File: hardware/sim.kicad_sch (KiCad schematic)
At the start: 11 parts, among them J14 PRPC006SAAN-RC, J15 G85D1160022HHR

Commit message: HW: Layout SIM section
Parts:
- removed J15: G85D1160022HHR, G85D1160022HHR:AMPHENOL_G85D1160022HHR, symbol Connector:SIM_Card
- added J15: G85D1160022HHR, G85D1160022HHR:AMPHENOL_G85D1160022HHR, symbol G85D1160022HHR:G85D1160022HHR
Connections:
- net GND: now also J15.C5 (GND), J15.S1 (SH), J15.S2 (SH), J15.S3 (SH)
- net SIM_CLK: now also J15.C3 (CLK)
- net SIM_IO: now also J15.C7 (I/O)
- net SIM_RST: now also J15.C2 (RST)
- net VSIM: now also J15.C1 (VCC)
- no-connect marks 1 -> 2
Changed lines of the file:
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@@
 	)
 	(junction
+		(at 187.96 134.62)
+		(diameter 0)
+		(color 0 0 0 0)
+	)
+	(junction
 		(at 182.88 119.38)
 		(diameter 0)
@@
 		(at 189.23 129.54)
 	)
+	(no_connect
+		(at 189.23 137.16)
+	)
 	(wire
 		(pts
@@
 	(wire
 		(pts
-			(xy 187.96 127) (xy 187.96 144.78)
+			(xy 187.96 127) (xy 187.96 134.62)
 		)
 		(stroke
@@
 	(wire
 		(pts
+			(xy 187.96 134.62) (xy 189.23 134.62)
+		)
+		(stroke
+			(width 0)
+			(type default)
+		)
+	)
+	(wire
+		(pts
 			(xy 189.23 127) (xy 187.96 127)
 		)
@@
 	(wire
 		(pts
+			(xy 187.96 134.62) (xy 187.96 144.78)
+		)
+		(stroke
+			(width 0)
+			(type default)
+		)
+	)
+	(wire
+		(pts
 			(xy 156.21 144.78) (xy 165.1 144.78)
 		)
@@
 	)
 	(symbol
-		(lib_id "Device:D_Zener")
-		(at 182.88 137.16 90)
-		(mirror x)
+		(lib_id "G85D1160022HHR:G85D1160022HHR")
+		(at 204.47 116.84 0)
 		(unit 1)
 		(exclude_from_sim no)
@@
 		(on_board yes)
 		(dnp no)
-		(property "Reference" "TVS15"
-			(at 178.435 137.16 90)
+		(property "Reference" "J15"
+			(at 202.692 116.84 0)
 			(effects
 				(font
 					(size 1.27 1.27)
 				)
+				(justify left)
 			)
 		)
-		(property "Value" "CPDUC5V0USP-HF"
-			(at 172.72 138.43 90)
+		(property "Value" "G85D1160022HHR"
+			(at 195.834 139.7 0)
 			(effects
 				(font
 					(size 1.27 1.27)
 				)
-				(hide yes)
+				(justify left)
 			)
 		)
-		(property "Footprint" "Diode_SMD:D_0603_1608Metric_Pad1.05x0.95mm_HandSolder"
-			(at 182.88 137.16 0)
+		(property "Footprint" "G85D1160022HHR:AMPHENOL_G85D1160022HHR"
+			(at 204.47 116.84 0)
 			(effects
 				(font
@@
 			)
 		)
-		(property "Datasheet" "~"
-			(at 182.88 137.16 0)
+		(property "Datasheet" "https://cdn.amphenol-cs.com/media/wysiwyg/files/drawing/g85d1160x22hhr.pdf"
+			(at 204.47 116.84 0)
 			(effects
 				(font
@@
 			)
 		)
-		(property "Description" ""
-			(at 182.88 137.16 0)
+		(property "Description" "NANO SIM HING GF"
+			(at 204.47 116.84 0)
 			(effects
 				(font
@@
 			)
 		)
-		(property "Digi-Key Part Number" "641-1765-1-ND"
-			(at 182.88 137.16 0)
+		(property "Digi-Key Part Number" "664-G85D1160022HHRCT-ND"
+			(at 204.47 116.84 0)
 			(effects
 				(font
@@
 			)
 		)
-		(property "Manufacturer" "Comchip Technology"
-			(at 182.88 137.16 0)
+		(property "Manufacturer" "Amphenol ICC (Commercial Products)"
+			(at 204.47 116.84 0)
 			(effects
 				(font
@@
 			)
 		)
-		(property "Manufacturer Part Number" "CPDUC5V0USP-HF"
-			(at 182.88 137.16 0)
+		(property "Manufacturer Part Number" "G85D1160022HHR"
+			(at 204.47 116.84 0)
 			(effects
 				(font
@@
 			)
 		)
-		(pin "2"
+		(pin "S2"
 		)
-		(pin "1"
+		(pin "C1"
+		)
+		(pin "C3"
+		)
+		(pin "C6"
+		)
+		(pin "C7"
+		)
+		(pin "SW"
+		)
+		(pin "C5"
+		)
+		(pin "S1"
+		)
+		(pin "S3"
+		)
+		(pin "C2"
 		)
 		(instances
-			(project "iida_devkit"
+			(project ""
 				(path "/b12a6e25-97fb-4aba-bc96-af8db389bb9a/33580d9f-a609-4568-baaf-9a29cf2dabcd"
-					(reference "TVS15")
+					(reference "J15")
 					(unit 1)
 				)
@@
 	(symbol
 		(lib_id "Device:D_Zener")
-		(at 156.21 137.16 90)
+		(at 182.88 137.16 90)
 		(mirror x)
 		(unit 1)
@@
 		(on_board yes)
 		(dnp no)
-		(property "Reference" "TVS12"
-			(at 151.765 137.16 90)
+		(property "Reference" "TVS15"
+			(at 178.435 137.16 90)
 			(effects
 				(font
@@
 		)
 		(property "Value" "CPDUC5V0USP-HF"
-			(at 146.05 138.43 90)
+			(at 172.72 138.43 90)
 			(effects
 				(font
@@
 		)
 		(property "Footprint" "Diode_SMD:D_0603_1608Metric_Pad1.05x0.95mm_HandSolder"
-			(at 156.21 137.16 0)
+			(at 182.88 137.16 0)
 			(effects
 				(font
@@
 		)
 		(property "Datasheet" "~"
-			(at 156.21 137.16 0)
+			(at 182.88 137.16 0)
 			(effects
 				(font
@@
 		)
 		(property "Description" ""
-			(at 156.21 137.16 0)
+			(at 182.88 137.16 0)
 			(effects
 				(font
@@
 		)
 		(property "Digi-Key Part Number" "641-1765-1-ND"
-			(at 156.21 137.16 0)
+			(at 182.88 137.16 0)
 			(effects
 				(font
@@
 		)
 		(property "Manufacturer" "Comchip Technology"
-			(at 156.21 137.16 0)
+			(at 182.88 137.16 0)
 			(effects
 				(font
@@
 		)
 		(property "Manufacturer Part Number" "CPDUC5V0USP-HF"
-			(at 156.21 137.16 0)
+			(at 182.88 137.16 0)
 			(effects
 				(font
@@
 			(project "iida_devkit"
 				(path "/b12a6e25-97fb-4aba-bc96-af8db389bb9a/33580d9f-a609-4568-baaf-9a29cf2dabcd"
-					(reference "TVS12")
+					(reference "TVS15")
 					(unit 1)
 				)
@@
 	)
 	(symbol
-		(lib_id "Device:C")
-		(at 121.92 137.16 0)
+		(lib_id "Device:D_Zener")
+		(at 156.21 137.16 90)
+		(mirror x)
 		(unit 1)
 		(exclude_from_sim no)
@@
 		(on_board yes)
 		(dnp no)
-		(property "Reference" "C35"
-			(at 119.38 135.89 0)
+		(property "Reference" "TVS12"
+			(at 151.765 137.16 90)
 			(effects
 				(font
 					(size 1.27 1.27)
 				)
-				(justify right)
 			)
 		)
-		(property "Value" "33 pF"
-			(at 119.38 138.43 0)
+		(property "Value" "CPDUC5V0USP-HF"
+			(at 146.05 138.43 90)
 			(effects
 				(font
 					(size 1.27 1.27)
 				)
-				(justify right)
+				(hide yes)
 			)
 		)
-		(property "Footprint" "Capacitor_SMD:C_0603_1608Metric_Pad1.08x0.95mm_HandSolder"
-			(at 122.8852 140.97 0)
+		(property "Footprint" "Diode_SMD:D_0603_1608Metric_Pad1.05x0.95mm_HandSolder"
+			(at 156.21 137.16 0)
 			(effects
 				(font
@@
 		)
 		(property "Datasheet" "~"
-			(at 121.92 137.16 0)
+			(at 156.21 137.16 0)
 			(effects
 				(font
@@
 		)
 		(property "Description" ""
-			(at 121.92 137.16 0)
+			(at 156.21 137.16 0)
 			(effects
 				(font
@@
 			)
 		)
-		(property "Digi-Key Part Number" "732-7749-1-ND"
-			(at 121.92 137.16 0)
+		(property "Digi-Key Part Number" "641-1765-1-ND"
+			(at 156.21 137.16 0)
 			(effects
 				(font
@@
 			)
 		)
-		(property "Manufacturer" "Würth Elektronik"
-			(at 121.92 137.16 0)
+		(property "Manufacturer" "Comchip Technology"
+			(at 156.21 137.16 0)
 			(effects
 				(font
@@
 			)
 		)
-		(property "Manufacturer Part Number" "885012006005"
-			(at 121.92 137.16 0)
+		(property "Manufacturer Part Number" "CPDUC5V0USP-HF"
+			(at 156.21 137.16 0)
 			(effects
 				(font
@@
 			(project "iida_devkit"
 				(path "/b12a6e25-97fb-4aba-bc96-af8db389bb9a/33580d9f-a609-4568-baaf-9a29cf2dabcd"
-					(reference "C35")
+					(reference "TVS12")
 					(unit 1)
 				)
@@
 	)
 	(symbol
-		(lib_id "Connector:SIM_Card")
-		(at 201.93 127 0)
+		(lib_id "Device:C")
+		(at 121.92 137.16 0)
 		(unit 1)
 		(exclude_from_sim no)
@@
 		(on_board yes)
 		(dnp no)
-		(property "Reference" "J15"
-			(at 204.47 114.808 0)
+		(property "Reference" "C35"
+			(at 119.38 135.89 0)
 			(effects
 				(font
 					(size 1.27 1.27)
 				)
+				(justify right)
 			)
 		)
-		(property "Value" "G85D1160022HHR"
-			(at 204.47 116.84 0)
+		(property "Value" "33 pF"
+			(at 119.38 138.43 0)
 			(effects
 				(font
 					(size 1.27 1.27)
 				)
+				(justify right)
 			)
 		)
-		(property "Footprint" "G85D1160022HHR:AMPHENOL_G85D1160022HHR"
-			(at 201.93 118.11 0)
+		(property "Footprint" "Capacitor_SMD:C_0603_1608Metric_Pad1.08x0.95mm_HandSolder"
+			(at 122.8852 140.97 0)
 			(effects
 				(font
@@
 		)
 		(property "Datasheet" "~"
-			(at 200.66 127 0)
+			(at 121.92 137.16 0)
 			(effects
 				(font
@@
 			)
 		)
-		(property "Description" "SIM Card"
-			(at 201.93 127 0)
+		(property "Description" ""
+			(at 121.92 137.16 0)
 			(effects
 				(font
@@
 			)
 		)
-		(property "Digi-Key Part Number" "664-G85D1160022HHRCT-ND"
-			(at 201.93 127 0)
+		(property "Digi-Key Part Number" "732-7749-1-ND"
+			(at 121.92 137.16 0)
 			(effects
 				(font
@@
 			)
 		)
-		(property "Manufacturer" "Amphenol ICC (Commercial Products)"
-			(at 201.93 127 0)
+		(property "Manufacturer" "Würth Elektronik"
+			(at 121.92 137.16 0)
 			(effects
 				(font
@@
 			)
 		)
-		(property "Manufacturer Part Number" "G85D1160022HHR"
-			(at 201.93 127 0)
+		(property "Manufacturer Part Number" "885012006005"
+			(at 121.92 137.16 0)
 			(effects
 				(font
@@
 			)
 		)
-		(pin "5"
-		)
-		(pin "7"
-		)
-		(pin "3"
-		)
 		(pin "2"
 		)
 		(pin "1"
 		)
-		(pin "6"
-		)
 		(instances
 			(project "iida_devkit"
 				(path "/b12a6e25-97fb-4aba-bc96-af8db389bb9a/33580d9f-a609-4568-baaf-9a29cf2dabcd"
-					(reference "J15")
+					(reference "C35")
 					(unit 1)
 				)

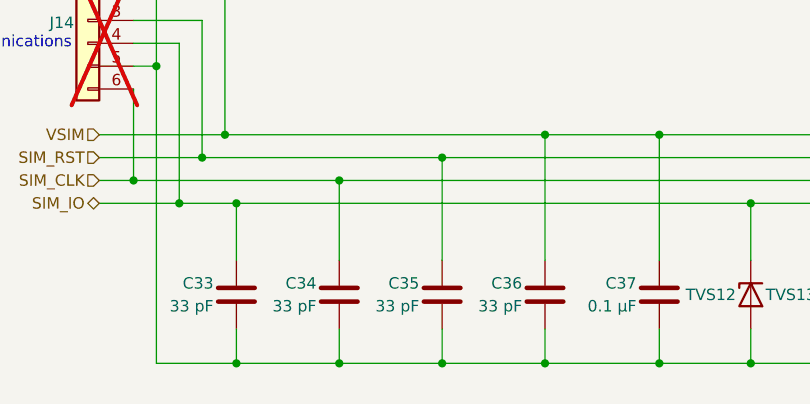
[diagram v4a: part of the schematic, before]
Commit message: HW: Add bulk cap to VBAT
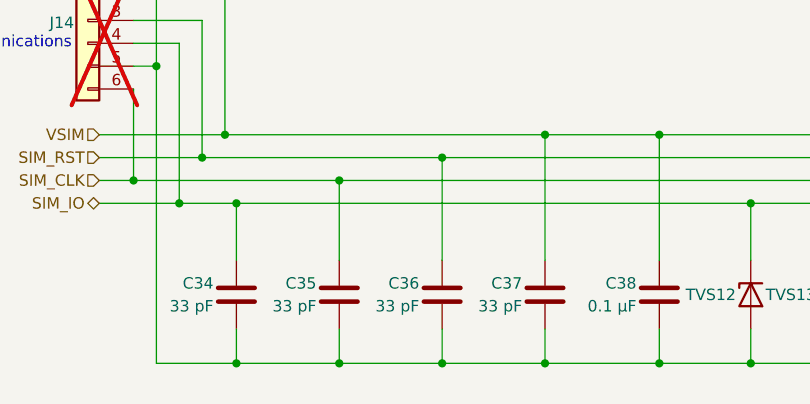
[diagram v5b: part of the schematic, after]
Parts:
- renumbered C33 to C34, C34 to C35, C35 to C36, C36 to C37, C37 to C38
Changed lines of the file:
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@@
 		(on_board yes)
 		(dnp no)
-		(property "Reference" "C37"
+		(property "Reference" "C38"
 			(at 143.51 135.89 0)
 			(effects
@@
 			(project "iida_devkit"
 				(path "/b12a6e25-97fb-4aba-bc96-af8db389bb9a/33580d9f-a609-4568-baaf-9a29cf2dabcd"
-					(reference "C37")
+					(reference "C38")
 					(unit 1)
 				)
@@
 		(on_board yes)
 		(dnp no)
-		(property "Reference" "C34"
+		(property "Reference" "C35"
 			(at 107.95 135.89 0)
 			(effects
@@
 			(project "iida_devkit"
 				(path "/b12a6e25-97fb-4aba-bc96-af8db389bb9a/33580d9f-a609-4568-baaf-9a29cf2dabcd"
-					(reference "C34")
+					(reference "C35")
 					(unit 1)
 				)
@@
 		(on_board yes)
 		(dnp no)
-		(property "Reference" "C33"
+		(property "Reference" "C34"
 			(at 96.52 135.89 0)
 			(effects
@@
 			(project "iida_devkit"
 				(path "/b12a6e25-97fb-4aba-bc96-af8db389bb9a/33580d9f-a609-4568-baaf-9a29cf2dabcd"
-					(reference "C33")
+					(reference "C34")
 					(unit 1)
 				)
@@
 		(on_board yes)
 		(dnp no)
-		(property "Reference" "C35"
+		(property "Reference" "C36"
 			(at 119.38 135.89 0)
 			(effects
@@
 			(project "iida_devkit"
 				(path "/b12a6e25-97fb-4aba-bc96-af8db389bb9a/33580d9f-a609-4568-baaf-9a29cf2dabcd"
-					(reference "C35")
+					(reference "C36")
 					(unit 1)
 				)
@@
 		(dnp no)
 		(fields_autoplaced yes)
-		(property "Reference" "#PWR052"
+		(property "Reference" "#PWR053"
 			(at 187.96 151.13 0)
 			(effects
@@
 			(project "iida_devkit"
 				(path "/b12a6e25-97fb-4aba-bc96-af8db389bb9a/33580d9f-a609-4568-baaf-9a29cf2dabcd"
-					(reference "#PWR052")
+					(reference "#PWR053")
 					(unit 1)
 				)
@@
 		(on_board yes)
 		(dnp no)
-		(property "Reference" "C36"
+		(property "Reference" "C37"
 			(at 130.81 135.89 0)
 			(effects
@@
 			(project "iida_devkit"
 				(path "/b12a6e25-97fb-4aba-bc96-af8db389bb9a/33580d9f-a609-4568-baaf-9a29cf2dabcd"
-					(reference "C36")
+					(reference "C37")
 					(unit 1)
 				)
